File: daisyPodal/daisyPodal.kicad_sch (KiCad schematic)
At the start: 39 parts, among them J1 Guitar in, J2 Left out, J3 fsw pin 1, J4 fsw pin 4, J5 fsw pin 6, J6 fsw pin 3, J7 fsw pin 2, J8 fsw pin 5, SW1 Switch 1, SW2 Switch 2, SW3 RotaryEncoder_Switch, U1 L78L05_TO92, U2 TL072

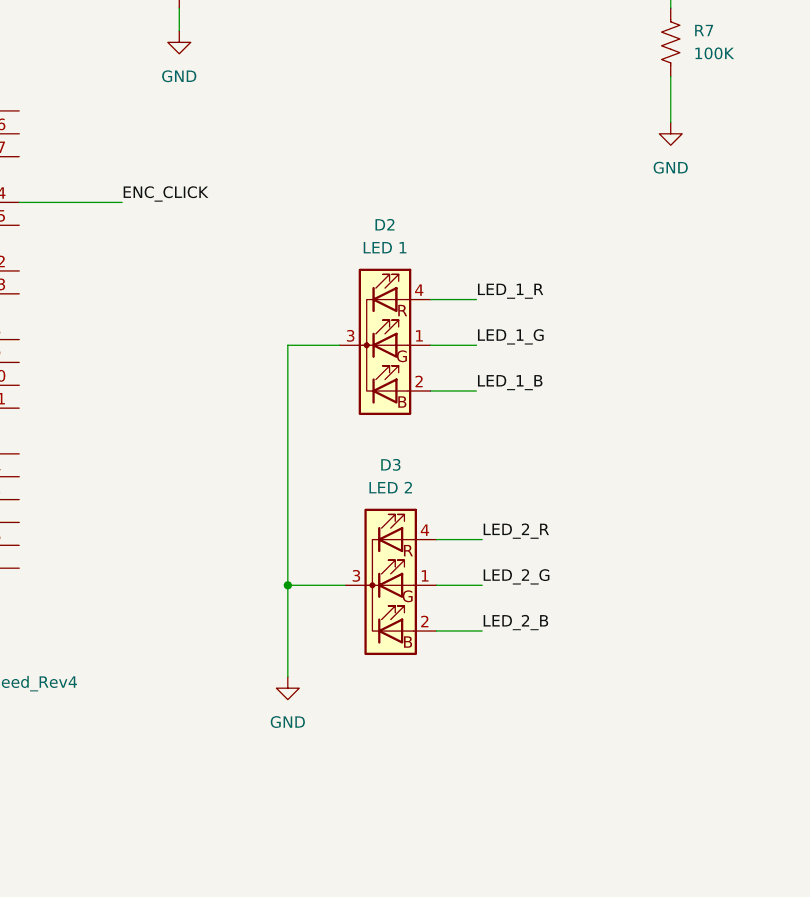
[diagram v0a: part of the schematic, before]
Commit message: Sort out correct RGB LEDS - RAGB
Common anode on the Pod
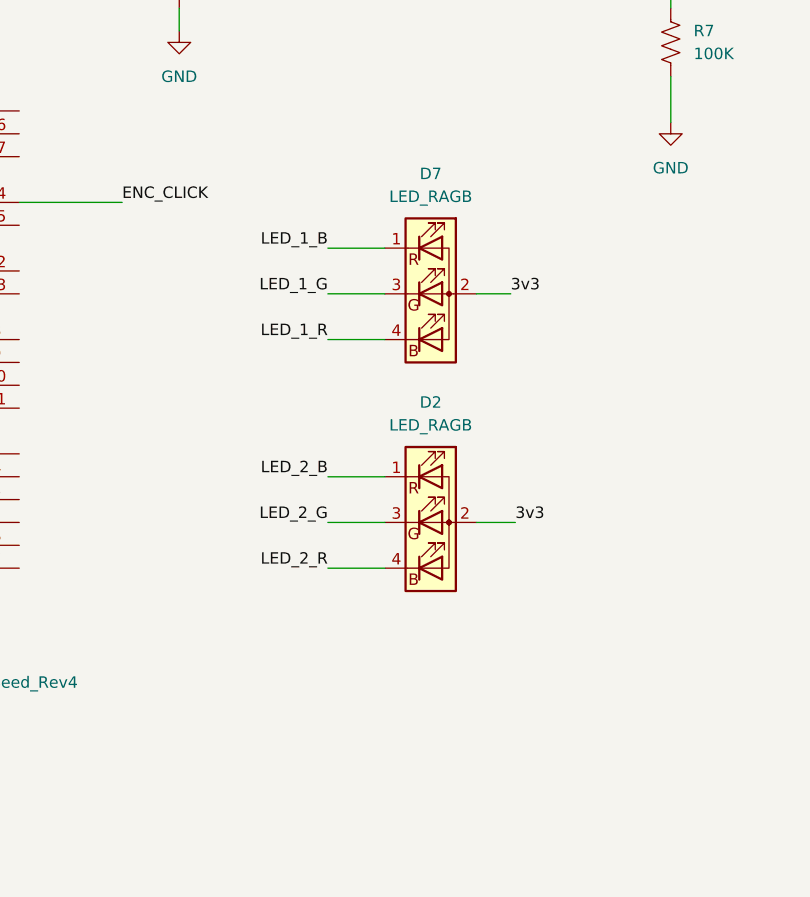
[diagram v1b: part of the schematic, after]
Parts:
- removed D2: LED 1, LED_THT:LED_D5.0mm-4_RGB, symbol Device:LED_GBKR
- removed D3: LED 2, LED_THT:LED_D5.0mm-4_RGB, symbol Device:LED_GBKR
- added D2, D7: LED_RAGB, symbol Device:LED_RAGB
- BT1: footprint Connector_BarrelJack:BarrelJack_Horizontal -> Connector_BarrelJack:BarrelJack_Horizontal_centre_negative
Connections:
- net 3v3: now also D2.2 (A), D7.2 (A)
- net LED_1_B: now also D7.1 (RK)
- net LED_1_G: now also D7.3 (GK)
- net LED_1_R: now also D7.4 (BK)
- net LED_2_B: now also D2.1 (RK)
- net LED_2_G: now also D2.3 (GK)
- net LED_2_R: now also D2.4 (BK)

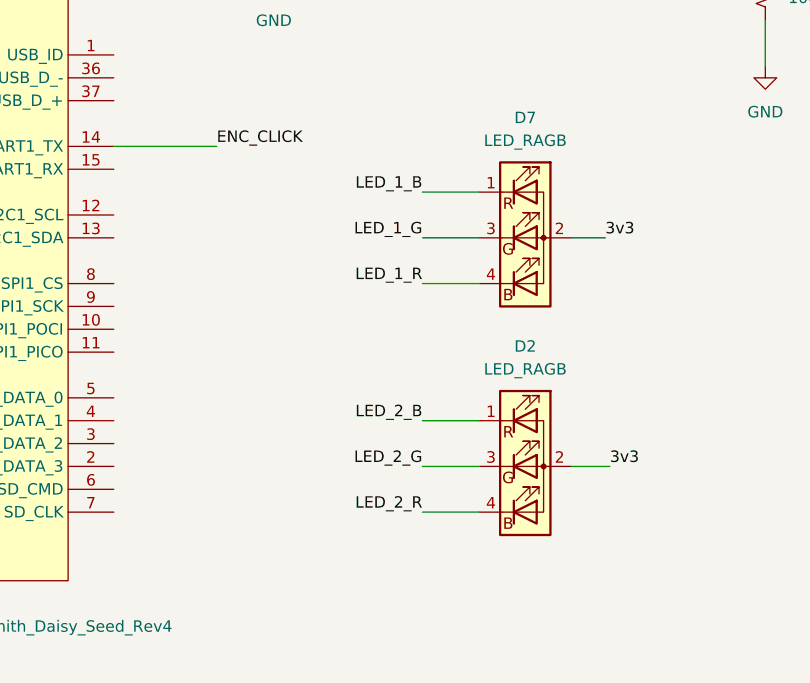
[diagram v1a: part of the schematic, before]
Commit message: With resistors for the RGB LEDs
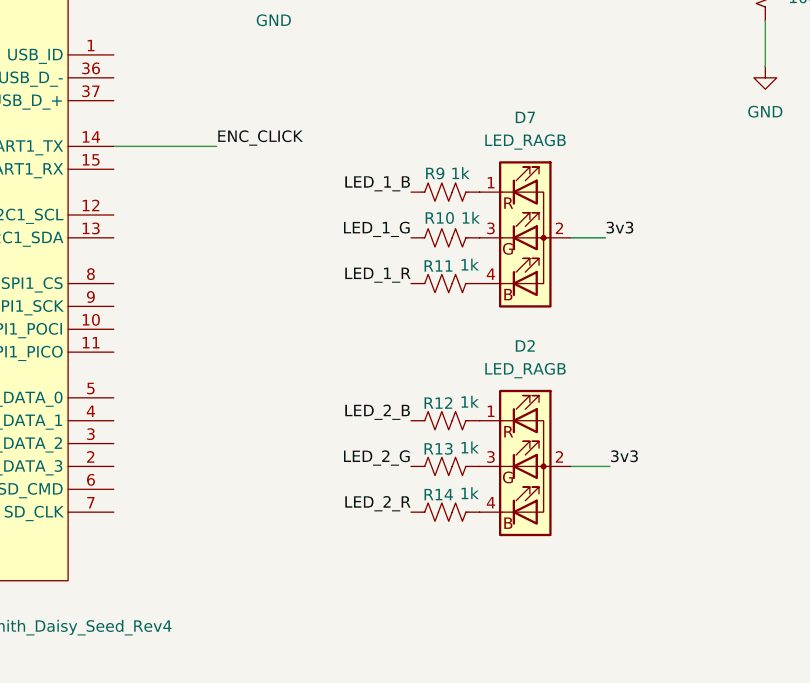
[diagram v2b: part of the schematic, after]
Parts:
- added R10, R11, R12, R13, R14, R9: 1k, Resistor_THT:R_Axial_DIN0207_L6.3mm_D2.5mm_P10.16mm_Horizontal, symbol Device:R_US
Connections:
- net LED_1_B: now also R9.1; no longer D7.1 (RK)
- net LED_1_G: now also R10.1; no longer D7.3 (GK)
- net LED_1_R: now also R11.1; no longer D7.4 (BK)
- net LED_2_B: now also R12.1; no longer D2.1 (RK)
- net LED_2_G: now also R13.1; no longer D2.3 (GK)
- net LED_2_R: now also R14.1; no longer D2.4 (BK)
- new net: D7.3 (GK), R10.2
- new net: D2.1 (RK), R12.2
- new net: D7.1 (RK), R9.2
- new net: D7.4 (BK), R11.2
- new net: D2.3 (GK), R13.2
- new net: D2.4 (BK), R14.2
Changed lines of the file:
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@@
-    (stroke (width 0) (type default))
-  )
-  (wire (pts (xy 222.25 120.65) (xy 228.6 120.65))
     (stroke (width 0) (type default))
   )
@@
     (stroke (width 0) (type default))
   )
-  (wire (pts (xy 222.25 125.73) (xy 228.6 125.73))
-    (stroke (width 0) (type default))
-  )
   (wire (pts (xy 132.08 125.73) (xy 137.16 125.73))
     (stroke (width 0) (type default))
@@
     (stroke (width 0) (type default))
   )
-  (wire (pts (xy 222.25 95.25) (xy 228.6 95.25))
-    (stroke (width 0) (type default))
-  )
   (wire (pts (xy 95.885 56.515) (xy 95.885 62.865))
     (stroke (width 0) (type default))
@@
     (stroke (width 0) (type default))
   )
-  (wire (pts (xy 222.25 100.33) (xy 228.6 100.33))
-    (stroke (width 0) (type default))
-  )
   (wire (pts (xy 132.08 132.08) (xy 127 132.08))
     (stroke (width 0) (type default))
@@
     (stroke (width 0) (type default))
   )
-  (wire (pts (xy 222.25 130.81) (xy 228.6 130.81))
-    (stroke (width 0) (type default))
-  )
   (wire (pts (xy 137.16 123.19) (xy 135.255 123.19))
     (stroke (width 0) (type default))
@@
   )
   (wire (pts (xy 134.62 120.65) (xy 137.16 120.65))
-    (stroke (width 0) (type default))
-  )
-  (wire (pts (xy 222.25 105.41) (xy 228.6 105.41))
     (stroke (width 0) (type default))
   )
@@
     (effects (font (size 1.27 1.27)) (justify right bottom))
   )
-  (label "LED_2_B" (at 222.25 120.65 180) (fields_autoplaced)
+  (label "LED_2_B" (at 220.98 120.65 180) (fields_autoplaced)
     (effects (font (size 1.27 1.27)) (justify right bottom))
   )
@@
     (effects (font (size 1.27 1.27)) (justify right bottom))
   )
-  (label "LED_2_R" (at 222.25 130.81 180) (fields_autoplaced)
+  (label "LED_2_R" (at 220.98 130.81 180) (fields_autoplaced)
     (effects (font (size 1.27 1.27)) (justify right bottom))
   )
-  (label "LED_2_G" (at 222.25 125.73 180) (fields_autoplaced)
+  (label "LED_2_G" (at 220.98 125.73 180) (fields_autoplaced)
     (effects (font (size 1.27 1.27)) (justify right bottom))
   )
@@
     (effects (font (size 1.27 1.27)) (justify left bottom))
   )
-  (label "LED_1_G" (at 222.25 100.33 180) (fields_autoplaced)
+  (label "LED_1_G" (at 220.98 100.33 180) (fields_autoplaced)
     (effects (font (size 1.27 1.27)) (justify right bottom))
   )
@@
     (effects (font (size 1.27 1.27)) (justify left bottom))
   )
-  (label "LED_1_R" (at 222.25 105.41 180) (fields_autoplaced)
+  (label "LED_1_R" (at 220.98 105.41 180) (fields_autoplaced)
     (effects (font (size 1.27 1.27)) (justify right bottom))
   )
@@
     (effects (font (size 1.27 1.27)) (justify left bottom))
   )
-  (label "LED_1_B" (at 222.25 95.25 180) (fields_autoplaced)
+  (label "LED_1_B" (at 220.98 95.25 180) (fields_autoplaced)
     (effects (font (size 1.27 1.27)) (justify right bottom))
+  )
+  (symbol (lib_id "Device:R_US") (at 224.79 100.33 90) (unit 1)
+    (in_bom yes) (on_board yes) (dnp no)
+    (property "Reference" "R10" (at 224.155 98.171 90)
+      (effects (font (size 1.27 1.27)))
+    )
+    (property "Value" "1k" (at 227.584 98.171 90)
+      (effects (font (size 1.27 1.27)))
+    )
+    (property "Footprint" "Resistor_THT:R_Axial_DIN0207_L6.3mm_D2.5mm_P10.16mm_Horizontal" (at 225.044 99.314 90)
+      (effects (font (size 1.27 1.27)) hide)
+    )
+    (property "Datasheet" "~" (at 224.79 100.33 0)
+      (effects (font (size 1.27 1.27)) hide)
+    )
+    (pin "1")
+    (pin "2")
+    (instances
+      (project "daisyPodal"
+        (path "/12e895f7-e5ae-4934-aed6-e6e04c63dd03"
+          (reference "R10") (unit 1)
+        )
+      )
+    )
+  )
+  (symbol (lib_id "Device:R_US") (at 224.79 120.65 90) (unit 1)
+    (in_bom yes) (on_board yes) (dnp no)
+    (property "Reference" "R12" (at 224.028 118.745 90)
+      (effects (font (size 1.27 1.27)))
+    )
+    (property "Value" "1k" (at 227.457 118.618 90)
+      (effects (font (size 1.27 1.27)))
+    )
+    (property "Footprint" "Resistor_THT:R_Axial_DIN0207_L6.3mm_D2.5mm_P10.16mm_Horizontal" (at 225.044 119.634 90)
+      (effects (font (size 1.27 1.27)) hide)
+    )
+    (property "Datasheet" "~" (at 224.79 120.65 0)
+      (effects (font (size 1.27 1.27)) hide)
+    )
+    (pin "1")
+    (pin "2")
+    (instances
+      (project "daisyPodal"
+        (path "/12e895f7-e5ae-4934-aed6-e6e04c63dd03"
+          (reference "R12") (unit 1)
+        )
+      )
+    )
   )
   (symbol (lib_id "Device:LED_RAGB") (at 233.68 100.33 0) (unit 1)
@@
         (path "/12e895f7-e5ae-4934-aed6-e6e04c63dd03"
           (reference "C10") (unit 1)
+        )
+      )
+    )
+  )
+  (symbol (lib_id "Device:R_US") (at 224.79 105.41 90) (unit 1)
+    (in_bom yes) (on_board yes) (dnp no)
+    (property "Reference" "R11" (at 224.028 103.505 90)
+      (effects (font (size 1.27 1.27)))
+    )
+    (property "Value" "1k" (at 227.457 103.378 90)
+      (effects (font (size 1.27 1.27)))
+    )
+    (property "Footprint" "Resistor_THT:R_Axial_DIN0207_L6.3mm_D2.5mm_P10.16mm_Horizontal" (at 225.044 104.394 90)
+      (effects (font (size 1.27 1.27)) hide)
+    )
+    (property "Datasheet" "~" (at 224.79 105.41 0)
+      (effects (font (size 1.27 1.27)) hide)
+    )
+    (pin "1")
+    (pin "2")
+    (instances
+      (project "daisyPodal"
+        (path "/12e895f7-e5ae-4934-aed6-e6e04c63dd03"
+          (reference "R11") (unit 1)
         )
       )
@@
     )
   )
+  (symbol (lib_id "Device:R_US") (at 224.79 125.73 90) (unit 1)
+    (in_bom yes) (on_board yes) (dnp no)
+    (property "Reference" "R13" (at 224.028 123.825 90)
+      (effects (font (size 1.27 1.27)))
+    )
+    (property "Value" "1k" (at 227.457 123.698 90)
+      (effects (font (size 1.27 1.27)))
+    )
+    (property "Footprint" "Resistor_THT:R_Axial_DIN0207_L6.3mm_D2.5mm_P10.16mm_Horizontal" (at 225.044 124.714 90)
+      (effects (font (size 1.27 1.27)) hide)
+    )
+    (property "Datasheet" "~" (at 224.79 125.73 0)
+      (effects (font (size 1.27 1.27)) hide)
+    )
+    (pin "1")
+    (pin "2")
+    (instances
+      (project "daisyPodal"
+        (path "/12e895f7-e5ae-4934-aed6-e6e04c63dd03"
+          (reference "R13") (unit 1)
+        )
+      )
+    )
+  )
   (symbol (lib_id "Device:C") (at 74.295 175.26 180) (unit 1)
     (in_bom yes) (on_board yes) (dnp no) (fields_autoplaced)
@@
         (path "/12e895f7-e5ae-4934-aed6-e6e04c63dd03"
           (reference "C1") (unit 1)
+        )
+      )
+    )
+  )
+  (symbol (lib_id "Device:R_US") (at 224.79 130.81 90) (unit 1)
+    (in_bom yes) (on_board yes) (dnp no)
+    (property "Reference" "R14" (at 224.028 128.905 90)
+      (effects (font (size 1.27 1.27)))
+    )
+    (property "Value" "1k" (at 227.457 128.778 90)
+      (effects (font (size 1.27 1.27)))
+    )
+    (property "Footprint" "Resistor_THT:R_Axial_DIN0207_L6.3mm_D2.5mm_P10.16mm_Horizontal" (at 225.044 129.794 90)
+      (effects (font (size 1.27 1.27)) hide)
+    )
+    (property "Datasheet" "~" (at 224.79 130.81 0)
+      (effects (font (size 1.27 1.27)) hide)
+    )
+    (pin "1")
+    (pin "2")
+    (instances
+      (project "daisyPodal"
+        (path "/12e895f7-e5ae-4934-aed6-e6e04c63dd03"
+          (reference "R14") (unit 1)
         )
       )
@@
         )
       )
+    )
+  )
+  (symbol (lib_id "Device:R_US") (at 224.79 95.25 90) (unit 1)
+    (in_bom yes) (on_board yes) (dnp no)
+    (property "Reference" "R9" (at 223.647 93.218 90)
+      (effects (font (size 1.27 1.27)))
+    )
+    (property "Value" "1k" (at 226.441 93.218 90)
+      (effects (font (size 1.27 1.27)))
+    )
+    (property "Footprint" "Resistor_THT:R_Axial_DIN0207_L6.3mm_D2.5mm_P10.16mm_Horizontal" (at 225.044 94.234 90)
+      (effects (font (size 1.27 1.27)) hide)
+    )
+    (property "Datasheet" "~" (at 224.79 95.25 0)
+      (effects (font (size 1.27 1.27)) hide)
+    )
+    (pin "1")
+    (pin "2")
+    (instances
+      (project "daisyPodal"
+        (path "/12e895f7-e5ae-4934-aed6-e6e04c63dd03"
+          (reference "R9") (unit 1)
+        )
+      )

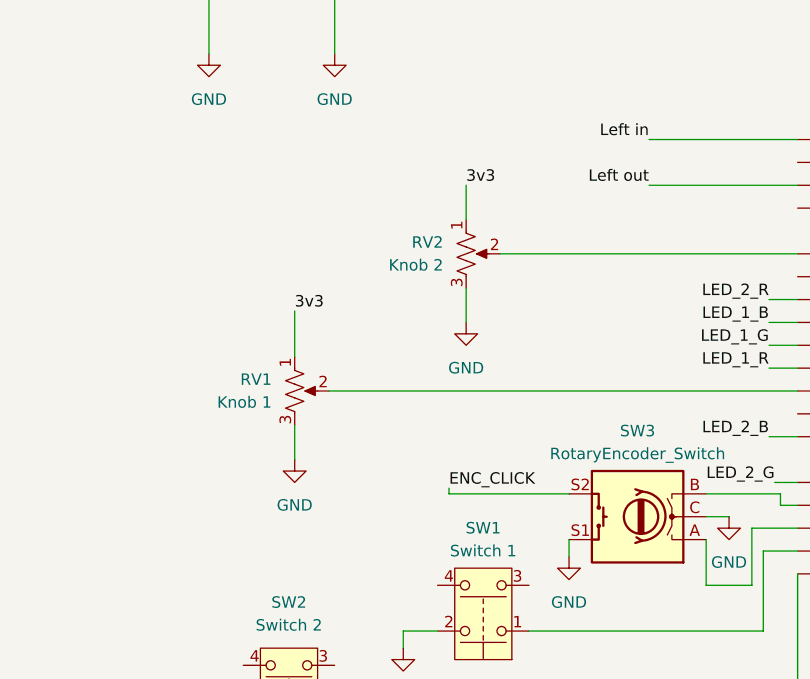
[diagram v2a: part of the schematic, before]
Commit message: Get the pots the right way around
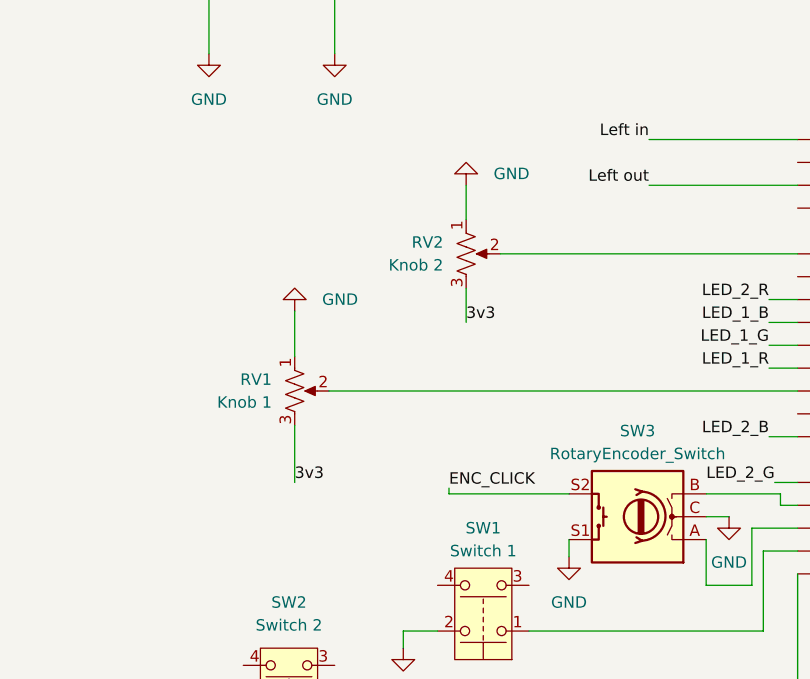
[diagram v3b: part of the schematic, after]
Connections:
- net 3v3: now also RV1.3, RV2.3; no longer RV1.1, RV2.1
- net GND: now also RV1.1, RV2.1; no longer RV1.3, RV2.3
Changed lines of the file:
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@@
     (stroke (width 0) (type default))
   )
-  (wire (pts (xy 81.28 114.3) (xy 81.28 118.11))
+  (wire (pts (xy 81.28 114.3) (xy 81.28 120.65))
     (stroke (width 0) (type default))
   )
@@
     (effects (font (size 1.27 1.27)) (justify right bottom))
   )
-  (label "3v3" (at 81.28 101.6 0) (fields_autoplaced)
+  (label "3v3" (at 81.28 120.65 0) (fields_autoplaced)
     (effects (font (size 1.27 1.27)) (justify left bottom))
   )
@@
     (effects (font (size 1.27 1.27)) (justify right bottom))
   )
-  (label "3v3" (at 100.33 87.63 0) (fields_autoplaced)
+  (label "3v3" (at 100.33 102.87 0) (fields_autoplaced)
     (effects (font (size 1.27 1.27)) (justify left bottom))
   )
@@
     )
   )
-  (symbol (lib_id "power:GND") (at 100.33 102.87 0) (unit 1)
-    (in_bom yes) (on_board yes) (dnp no) (fields_autoplaced)
-    (property "Reference" "#PWR022" (at 100.33 109.22 0)
-      (effects (font (size 1.27 1.27)) hide)
-    )
-    (property "Value" "GND" (at 100.33 107.95 0)
-      (effects (font (size 1.27 1.27)))
-    )
-    (property "Footprint" "" (at 100.33 102.87 0)
-      (effects (font (size 1.27 1.27)) hide)
-    )
-    (property "Datasheet" "" (at 100.33 102.87 0)
+  (symbol (lib_id "power:GND") (at 100.33 87.63 180) (unit 1)
+    (in_bom yes) (on_board yes) (dnp no) (fields_autoplaced)
+    (property "Reference" "#PWR022" (at 100.33 81.28 0)
+      (effects (font (size 1.27 1.27)) hide)
+    )
+    (property "Value" "GND" (at 103.378 86.36 0)
+      (effects (font (size 1.27 1.27)) (justify right))
+    )
+    (property "Footprint" "" (at 100.33 87.63 0)
+      (effects (font (size 1.27 1.27)) hide)
+    )
+    (property "Datasheet" "" (at 100.33 87.63 0)
       (effects (font (size 1.27 1.27)) hide)
     )
@@
     )
   )
-  (symbol (lib_id "power:GND") (at 81.28 118.11 0) (unit 1)
-    (in_bom yes) (on_board yes) (dnp no) (fields_autoplaced)
-    (property "Reference" "#PWR021" (at 81.28 124.46 0)
-      (effects (font (size 1.27 1.27)) hide)
-    )
-    (property "Value" "GND" (at 81.28 123.19 0)
-      (effects (font (size 1.27 1.27)))
-    )
-    (property "Footprint" "" (at 81.28 118.11 0)
-      (effects (font (size 1.27 1.27)) hide)
-    )
-    (property "Datasheet" "" (at 81.28 118.11 0)
-      (effects (font (size 1.27 1.27)) hide)
-    )
+  (symbol (lib_id "power:GND") (at 81.28 101.6 180) (unit 1)
+    (in_bom yes) (on_board yes) (dnp no) (fields_autoplaced)
+    (property "Reference" "#PWR021" (at 81.28 95.25 0)
+      (effects (font (size 1.27 1.27)) hide)
+    )
+    (property "Value" "GND" (at 84.328 100.33 0)
+      (effects (font (size 1.27 1.27)) (justify right))
+    )
+    (property "Footprint" "" (at 81.28 101.6 0)
+      (effects (font (size 1.27 1.27)) hide)
+    )
+    (property "Datasheet" "" (at 81.28 101.6 0)
+      (effects (font (size 1.27 1.27)) hide)
+    )
